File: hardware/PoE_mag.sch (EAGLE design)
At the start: 129 parts, among them IC1 LD1117V33, IC10 74LVC1T45SOT23-HAND, IC11 74LVC1T45SOT23-HAND, IC12 PCA9517A, IC2 LD1117V33, IC3 DS1338, IC4 ATMEGA1284, IC5 TSR 1-2450, IC6 LM61, IC7 MCP2200, IC8 74LVC1T45SOT23-HAND, IC9 74LVC1T45SOT23-HAND, Q1 BSS138, Q2 BUK98150-55A, X1 PWR, X2 JTAG, X3 USB, X4 MICRO-SD-SOCKETHIROSE-DM3D, X5 CONN-SMATHD, X6 UFL, X7 22-23-2021, X8 RJ45, X9 RJ11, Y1 32k768, Y2 12MHz, Y3 12MHz

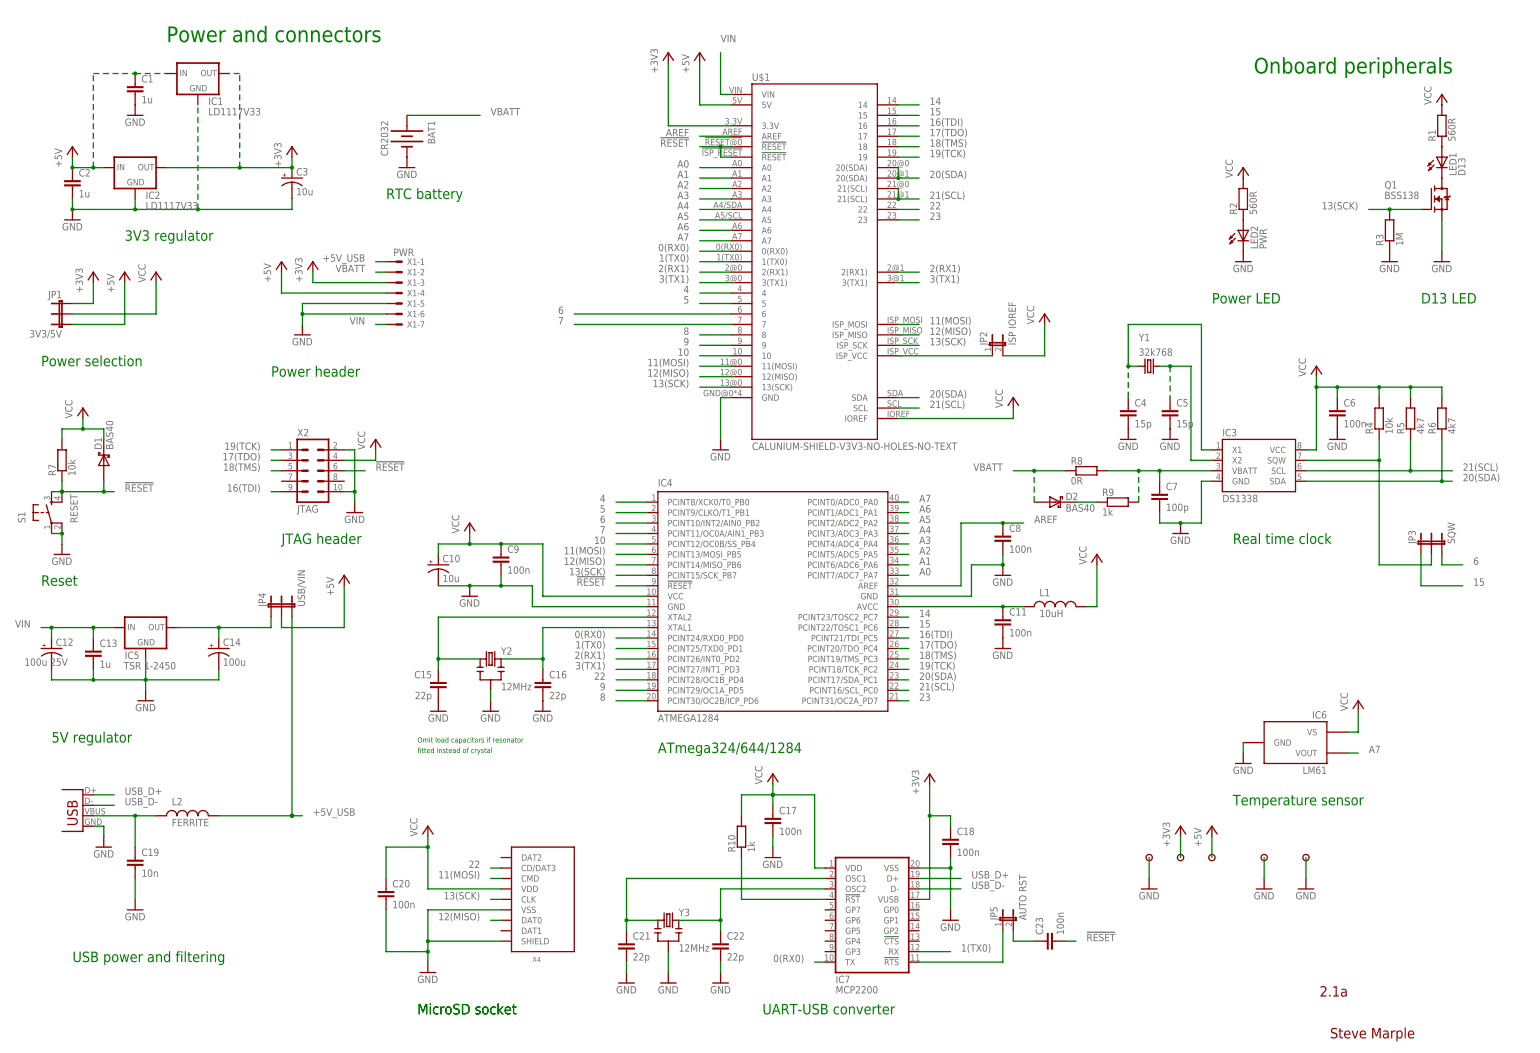
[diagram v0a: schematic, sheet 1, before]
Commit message: Show alternative build configurations more clearly
Move TO-220 variant of LD1117V33 to show it is the alternative
fit. Use short dashed lines to connect all optional/variant
components. Add "*" suffix to component values which are
optional/variants to ease construction o the standard version. Minor
silkscreen changes on board to accomodate longer text.
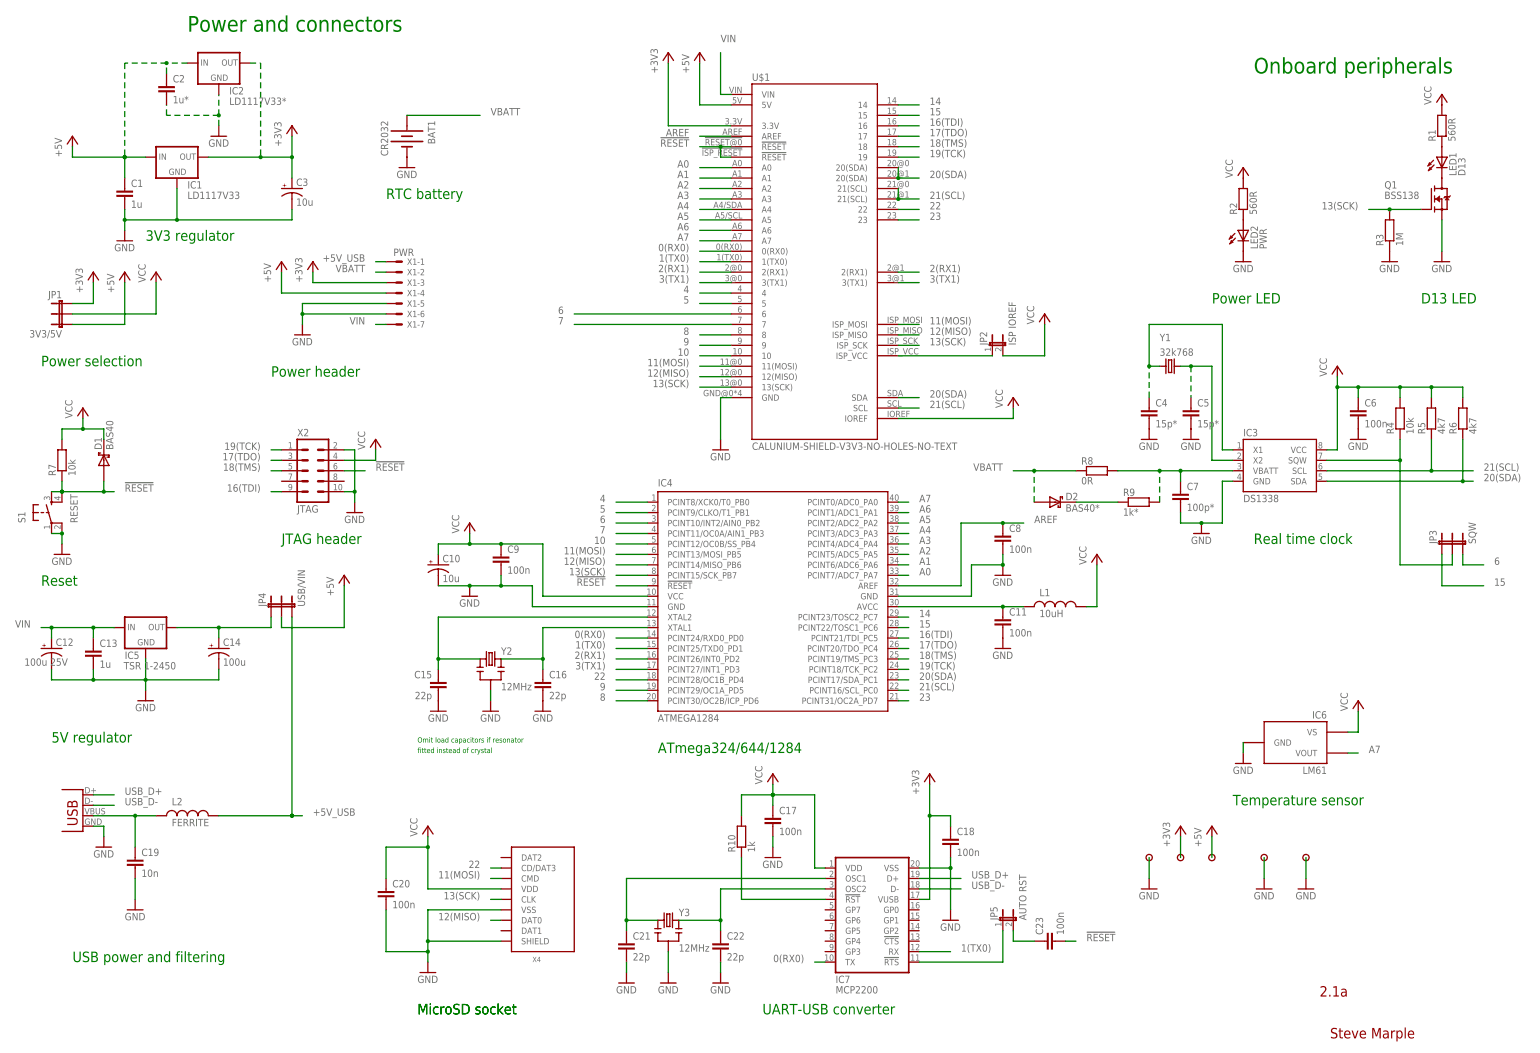
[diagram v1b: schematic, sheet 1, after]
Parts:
- C2: value 1u -> 1u*
- C4, C5: value 15p -> 15p*
- C7: value 100p -> 100p*
- D2: value BAS40 -> BAS40*
- IC2: value LD1117V33 -> LD1117V33*
- R9: value 1k -> 1k*
- X8: value RJ45 -> RJ45*
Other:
- note added: "Voltage selection for battery or power-over-ethernet operation. Fit only when RJ45 jack fitted."
- note removed: "Voltage selection for battery or power-over-ethernet operation."
- moved on the sheet: C1, C2, C3, C4, C5, C6, C7, IC1, IC2, IC3, JP3, R4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

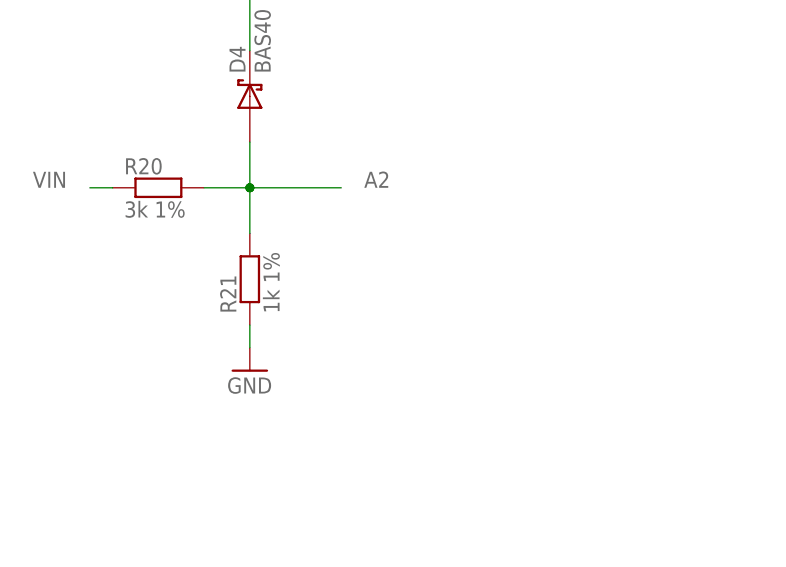
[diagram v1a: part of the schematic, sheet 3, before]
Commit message: Add decoupling for supply voltage measurement
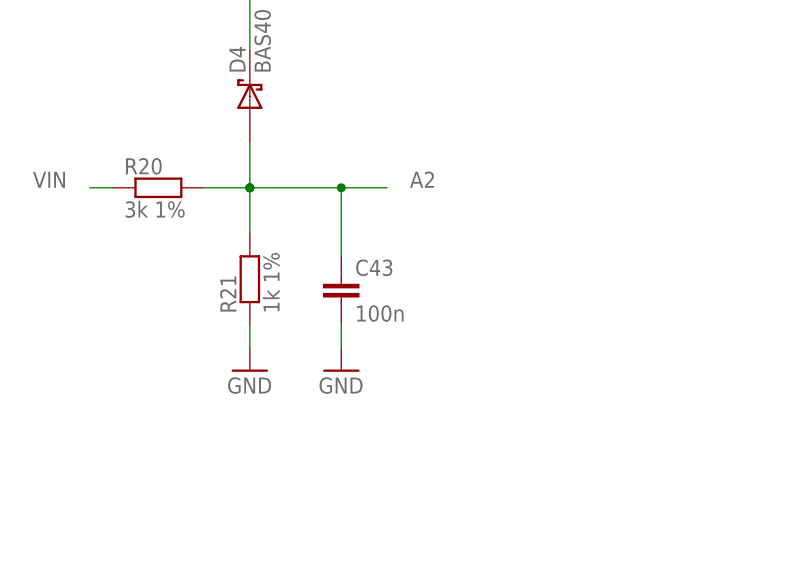
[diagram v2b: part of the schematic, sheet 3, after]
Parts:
- added C43: 100n, SteveMarple:C-EU1206-HAND
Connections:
- net A2: now also C43.1
- net GND: now also C43.2
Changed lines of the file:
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@@
 <part name="GND51" library="supply1" deviceset="GND" device=""/>
 <part name="C42" library="SteveMarple" deviceset="C-EU" device="1206-HAND" value="1u"/>
+<part name="C43" library="SteveMarple" deviceset="C-EU" device="1206-HAND" value="100n"/>
+<part name="GND52" library="supply1" deviceset="GND" device=""/>
 </parts>
 <sheets>
@@
 <junction x="127" y="53.34"/>
 <pinref part="C7" gate="G$1" pin="2"/>
-<wire x1="121.92" y1="55.88" x2="121.92" y2="53.34" width="0.1524" layer="91"/>
-<wire x1="121.92" y1="53.34" x2="127" y2="53.34" width="0.1524" layer="91"/>
+<wire x1="121.92" y1="55.88" x2="121.92" y2="53.34" width="0.1524" layer="91" style="shortdash"/>
+<wire x1="121.92" y1="53.34" x2="127" y2="53.34" width="0.1524" layer="91" style="shortdash"/>
 </segment>
 <segment>
@@
 <pinref part="C7" gate="G$1" pin="1"/>
 <junction x="121.92" y="66.04"/>
-<wire x1="121.92" y1="63.5" x2="121.92" y2="66.04" width="0.1524" layer="91"/>
+<wire x1="121.92" y1="63.5" x2="121.92" y2="66.04" width="0.1524" layer="91" style="shortdash"/>
 <junction x="116.84" y="66.04"/>
 <pinref part="R8" gate="G$1" pin="2"/>
@@
 <instance part="P+19" gate="VCC" x="58.42" y="81.28"/>
 <instance part="C42" gate="G$1" x="88.9" y="210.82"/>
+<instance part="C43" gate="G$1" x="68.58" y="45.72"/>
+<instance part="GND52" gate="1" x="68.58" y="35.56"/>
 </instances>
 <busses>
@@
 <pinref part="GND44" gate="1" pin="GND"/>
 <wire x1="58.42" y1="40.64" x2="58.42" y2="38.1" width="0.1524" layer="91"/>
+</segment>
+<segment>
+<pinref part="C43" gate="G$1" pin="2"/>
+<pinref part="GND52" gate="1" pin="GND"/>
+<wire x1="68.58" y1="40.64" x2="68.58" y2="38.1" width="0.1524" layer="91"/>
 </segment>
 </net>
@@
 <net name="A2" class="0">
 <segment>
-<wire x1="68.58" y1="55.88" x2="58.42" y2="55.88" width="0.1524" layer="91"/>
-<label x="71.12" y="55.88" size="1.778" layer="95"/>
+<wire x1="73.66" y1="55.88" x2="68.58" y2="55.88" width="0.1524" layer="91"/>
+<label x="76.2" y="55.88" size="1.778" layer="95"/>
 <junction x="58.42" y="55.88"/>
 <pinref part="R20" gate="G$1" pin="2"/>
+<wire x1="68.58" y1="55.88" x2="58.42" y2="55.88" width="0.1524" layer="91"/>
 <wire x1="53.34" y1="55.88" x2="58.42" y2="55.88" width="0.1524" layer="91"/>
 <junction x="58.42" y="55.88"/>
@@
 <pinref part="D4" gate="G$1" pin="A"/>
 <wire x1="58.42" y1="60.96" x2="58.42" y2="55.88" width="0.1524" layer="91"/>
-</segment>
-</net>
+<junction x="68.58" y="55.88"/>
+<pinref part="C43" gate="G$1" pin="1"/>
+<wire x1="68.58" y1="55.88" x2="68.58" y2="48.26" width="0.1524" layer="91"/>
+</segment>
+</net>
